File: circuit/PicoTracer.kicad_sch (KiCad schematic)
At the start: 16 parts, among them J1 Conn_01x04_Socket, J2 Conn_01x04_Socket, J6 Conn_01x04_Socket, J7 8P8C, SW1 SW_Push, SW2 SW_Push, U1 Pico, U2 MCP3002, U3 MCP3002

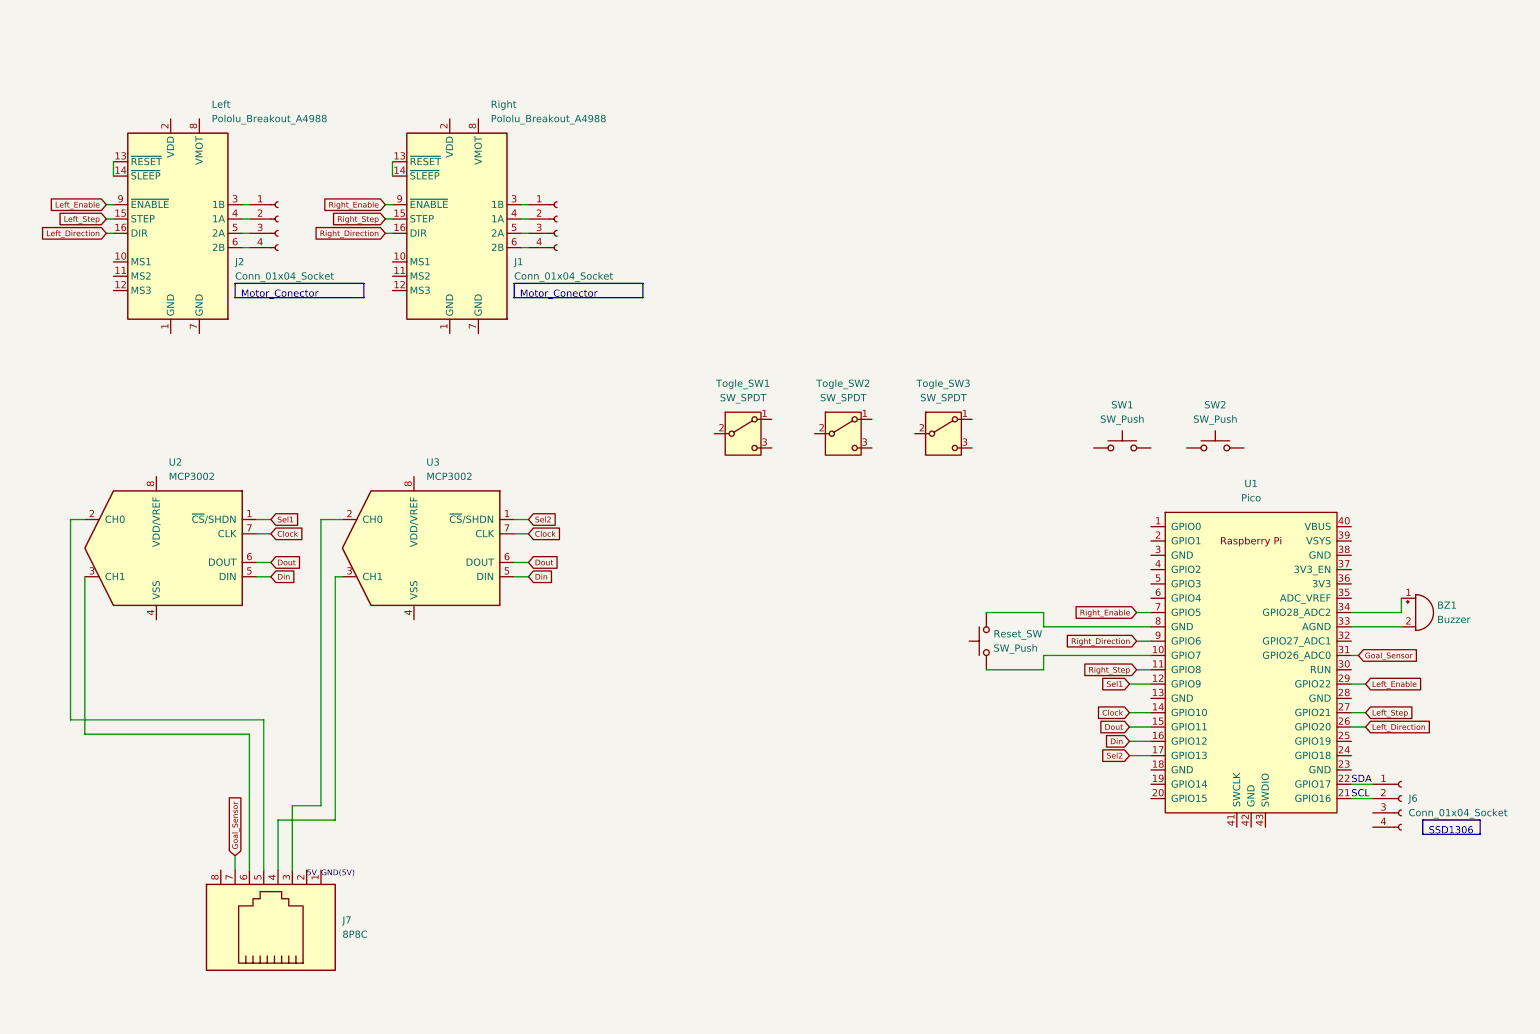
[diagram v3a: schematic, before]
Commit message: 電源周り追加、プッシュスイッチ追加、電圧計測回路追加、センサー回路追加
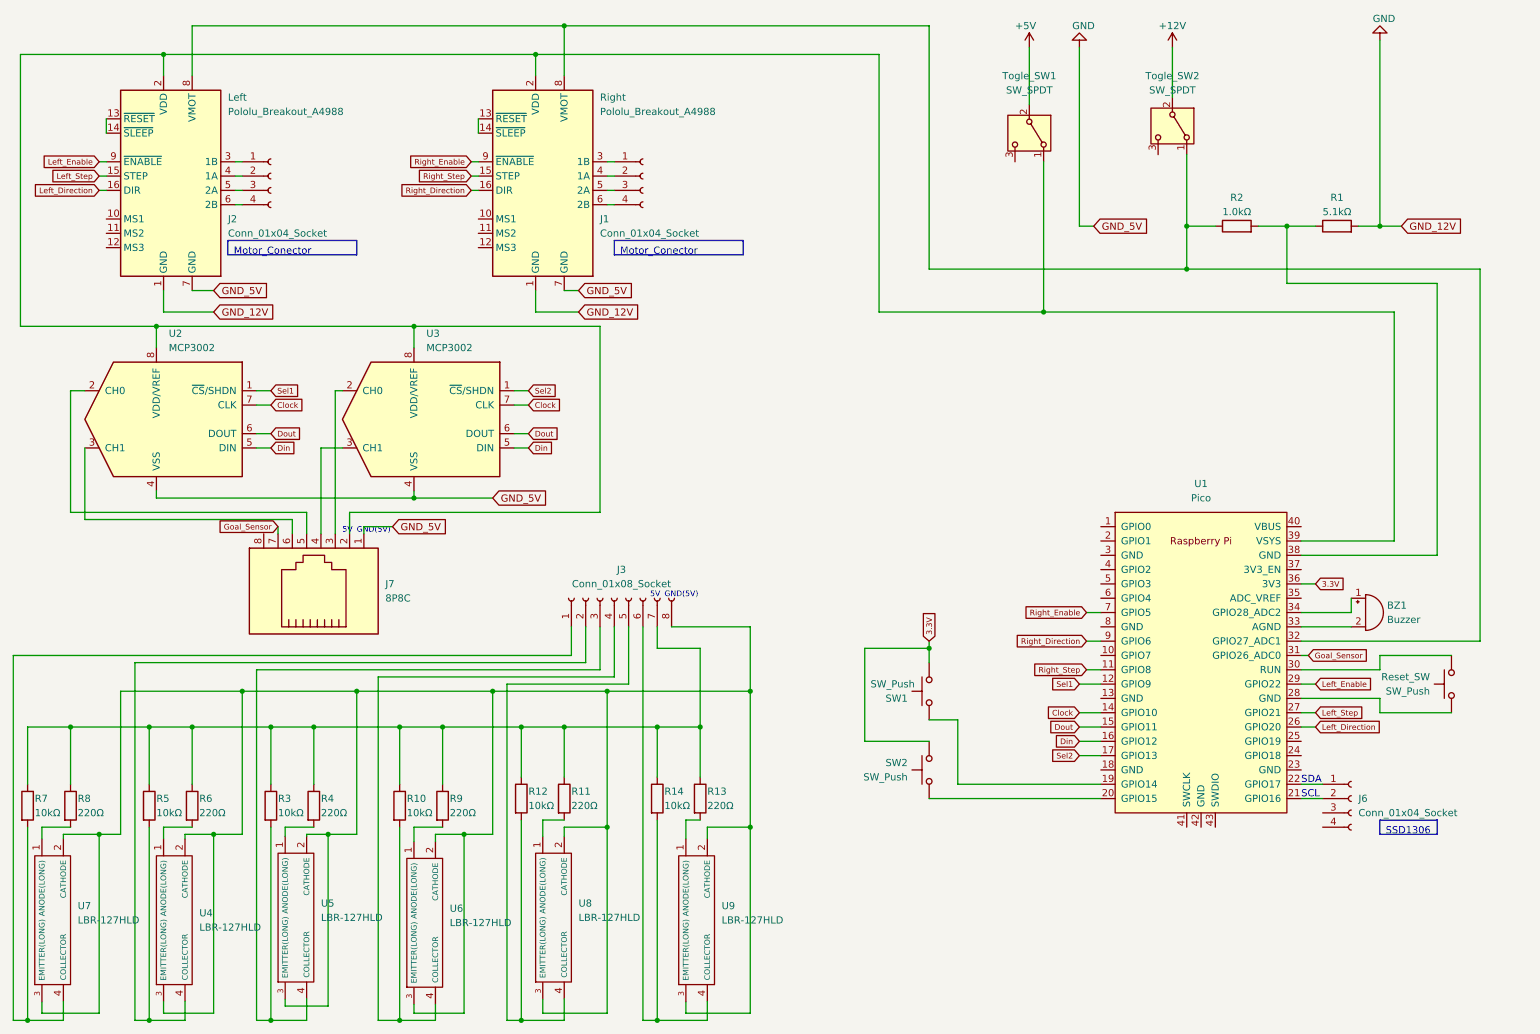
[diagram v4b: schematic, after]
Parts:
- removed Togle_SW3: SW_SPDT, symbol Switch:SW_SPDT
- added J3: Conn_01x08_Socket, symbol Connector:Conn_01x08_Socket
- added R1: 5.1kΩ, symbol Device:R
- added R10, R12, R14, R3, R5, R7: 10kΩ, symbol Device:R
- added R11, R13, R4, R6, R8, R9: 220Ω, symbol Device:R
- added R2: 1.0kΩ, symbol Device:R
- added U4, U5, U6, U7, U8, U9: LBR-127HLD, LBR127HLD, symbol SamacSys_Parts:LBR-127HLD
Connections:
- net 3.3V: now reaches SW2.1
- net 3.3V: now also SW1.2, U1.36 (3V3)
- net at SW2.2: now also U1.20 (GPIO15)
- net at U1.10 (GPIO7): no longer Reset_SW.1
- net at Reset_SW.2: now also U1.28 (GND); no longer U1.8 (GND)
- net GND: now reaches J7.1
- net GND: now also Left.1 (GND), Left.7 (GND), Right.1 (GND), Right.7 (GND), U2.4 (VSS), U3.4 (VSS), R1.2
- net at J7.2: now also Left.2 (VDD), Right.2 (VDD), Togle_SW1.1 (A), U1.39 (VSYS), U2.8 (VDD/VREF), U3.8 (VDD/VREF)
- net at U1.19 (GPIO14): now also SW1.1
- net at U1.30 (RUN): now also Reset_SW.1
- net at U1.32 (GPIO27_ADC1): now also Left.8 (VMOT), Right.8 (VMOT), Togle_SW2.1 (A), R2.1
- net at U1.38 (GND): now also R1.1, R2.2
- net +5V: now reaches Togle_SW1.2 (B)
- net +12V: now reaches Togle_SW2.2 (B)
- new net: R13.2, U9.1 (ANODE(LONG))
- new net: J3.8 (Pin_8), U4.2 (CATHODE), U4.3 (EMITTER(LONG)), U5.2 (CATHODE), U5.3 (EMITTER(LONG)), U6.2 (CATHODE), U6.3 (EMITTER(LONG)), U7.2 (CATHODE), U7.3 (EMITTER(LONG)), U8.2 (CATHODE), U8.3 (EMITTER(LONG)), U9.2 (CATHODE), U9.3 (EMITTER(LONG))
- new net: J3.6 (Pin_6), R14.2, U9.4 (COLLECTOR)
- new net: J3.7 (Pin_7), R10.1, R11.1, R12.1, R13.1, R14.1, R3.1, R4.1, R5.1, R6.1, R7.1, R8.1, R9.1
- new net: J3.4 (Pin_4), R10.2, U6.4 (COLLECTOR)
- new net: J3.2 (Pin_2), R5.2, U4.4 (COLLECTOR)
- new net: J3.3 (Pin_3), R3.2, U5.4 (COLLECTOR)
- new net: R6.2, U4.1 (ANODE(LONG))
- new net: R8.2, U7.1 (ANODE(LONG))
- new net: R4.2, U5.1 (ANODE(LONG))
- new net: R11.2, U8.1 (ANODE(LONG))
- new net: J3.5 (Pin_5), R12.2, U8.4 (COLLECTOR)
- new net: R9.2, U6.1 (ANODE(LONG))
- new net: J3.1 (Pin_1), R7.2, U7.4 (COLLECTOR)
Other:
- moved on the sheet: BZ1, J1, J2, J6, J7, Left, Right, Togle_SW1, Togle_SW2, U1, U2, U3
